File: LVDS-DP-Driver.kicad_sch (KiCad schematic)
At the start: 122 parts, among them J1 47272-0001, J2 Conn_02x15_Odd_Even, J3 Conn_01x06_Male, J4 Conn_01x03_Male, J5 Conn_01x04_Male, J6 Conn_01x03_Male, Q1 Si4816BDY, Q10 2N7002, Q2 Si4816BDY, Q3 Si4816BDY, Q4 MMBT3904, Q5 MMBT3904, Q6 2N7002, Q7 AO3401A, Q8 2N7002, Q9 2N7002, SW1 SW_DIP_x04, U1 CS5211, U2 LTC3853, U3 AT24C64

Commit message: created subschem and C project
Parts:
- J1: footprint Footprints:MOLEX_47272-0001 -> MOLEX_47272-0001
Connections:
- net +3V3 is gone; now on net +3.3V: C10.2, C11.1, C12.1, C37.1, C38.1, C39.1, L1.2, R8.2, R9.1, U1.18 (LVDD), U1.32 (LVDD), U1.52 (LVDD), U2.6 (SENSE2-)
- net GND: no longer SW1.5, SW1.6, SW1.7, U1.63 (GND)
- net GPIO1: no longer SW1.2
- net GPIO2: no longer SW1.3
- net GPIO3: no longer SW1.4
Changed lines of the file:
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@@
   (junction (at 93.345 85.09) (diameter 0) (color 0 0 0 0)
   )
-  (junction (at 212.09 143.51) (diameter 0) (color 0 0 0 0)
-  )
   (junction (at 264.16 105.41) (diameter 0) (color 0 0 0 0)
   )
@@
   (junction (at 33.02 66.04) (diameter 0) (color 0 0 0 0)
   )
-  (junction (at 212.09 139.7) (diameter 0) (color 0 0 0 0)
-  )
-  (junction (at 212.09 141.605) (diameter 0) (color 0 0 0 0)
-  )
   (junction (at 269.24 108.585) (diameter 0) (color 0 0 0 0)
   )
@@
     (stroke (width 0) (type default))
   )
-  (wire (pts (xy 212.09 137.795) (xy 212.09 139.7))
-    (stroke (width 0) (type default))
-  )
   (wire (pts (xy 212.09 78.105) (xy 212.09 84.455))
     (stroke (width 0) (type default))
@@
     (stroke (width 0) (type default))
   )
-  (wire (pts (xy 212.09 141.605) (xy 212.09 143.51))
-    (stroke (width 0) (type default))
-  )
-  (wire (pts (xy 212.09 139.7) (xy 212.09 141.605))
+  (wire (pts (xy 212.09 137.795) (xy 212.09 143.51))
     (stroke (width 0) (type default))
   )
@@
     )
   )
-  (symbol (lib_name "+3.3V_6") (lib_id "power:+3.3V") (at 93.345 85.09 90) (unit 1)
+  (symbol (lib_id "power:+3.3V") (at 93.345 85.09 90) (unit 1)
     (in_bom yes) (on_board yes) (dnp no)
     (property "Reference" "#PWR031" (at 97.155 85.09 0)
@@
     )
   )
-  (symbol (lib_name "+3.3V_7") (lib_id "power:+3.3V") (at 108.585 77.47 0) (unit 1)
+  (symbol (lib_id "power:+3.3V") (at 108.585 77.47 0) (unit 1)
     (in_bom yes) (on_board yes) (dnp no)
     (property "Reference" "#PWR032" (at 108.585 81.28 0)
@@
     (pin "46")
     (pin "47")
-    (pin "47")
     (pin "48")
     (pin "49")
@@
     (pin "52")
     (pin "60")
-    (pin "63")
     (pin "66")
     (pin "67")
@@
     )
   )
-  (symbol (lib_name "+3.3V_4") (lib_id "power:+3.3V") (at 31.115 179.07 0) (unit 1)
+  (symbol (lib_id "power:+3.3V") (at 31.115 179.07 0) (unit 1)
     (in_bom yes) (on_board yes) (dnp no) (fields_autoplaced)
     (property "Reference" "#PWR028" (at 31.115 182.88 0)
@@
     )
   )
-  (symbol (lib_name "+3.3V_3") (lib_id "power:+3.3V") (at 23.495 97.155 270) (unit 1)
+  (symbol (lib_id "power:+3.3V") (at 23.495 97.155 270) (unit 1)
     (in_bom yes) (on_board yes) (dnp no)
     (property "Reference" "#PWR022" (at 19.685 97.155 0)
@@
     )
   )
-  (symbol (lib_name "+3.3V_1") (lib_id "power:+3.3V") (at 160.02 120.65 0) (unit 1)
+  (symbol (lib_id "power:+3.3V") (at 160.02 120.65 0) (unit 1)
     (in_bom yes) (on_board yes) (dnp no)
     (property "Reference" "#PWR0127" (at 160.02 124.46 0)
@@
     )
   )
-  (symbol (lib_name "+3.3V_1") (lib_id "power:+3.3V") (at 133.985 120.65 0) (unit 1)
+  (symbol (lib_id "power:+3.3V") (at 133.985 120.65 0) (unit 1)
     (in_bom yes) (on_board yes) (dnp no)
     (property "Reference" "#PWR0129" (at 133.985 124.46 0)
@@
     )
   )
-  (symbol (lib_name "+3.3V_2") (lib_id "power:+3.3V") (at 31.75 158.115 0) (unit 1)
+  (symbol (lib_id "power:+3.3V") (at 31.75 158.115 0) (unit 1)
     (in_bom yes) (on_board yes) (dnp no) (fields_autoplaced)
     (property "Reference" "#PWR021" (at 31.75 161.925 0)
@@
     )
   )
-  (symbol (lib_name "+3.3V_5") (lib_id "power:+3.3V") (at 81.28 170.815 0) (unit 1)
+  (symbol (lib_id "power:+3.3V") (at 81.28 170.815 0) (unit 1)
     (in_bom yes) (on_board yes) (dnp no) (fields_autoplaced)
     (property "Reference" "#PWR029" (at 81.28 174.625 0)
@@
       (effects (font (size 1.27 1.27)))
     )
-    (property "Footprint" "Footprints:MOLEX_47272-0001" (at 19.05 45.72 0)
+    (property "Footprint" "MOLEX_47272-0001" (at 19.05 45.72 0)
       (effects (font (size 1.27 1.27)) (justify right bottom) hide)
     )
@@
       (project "LVDS-DP-Driver"
         (path "/46838880-46e6-40b4-8167-4d1ff56fb624"
-          (reference "J1") (unit 1) (value "47272-0001") (footprint "Footprints:MOLEX_47272-0001")
+          (reference "J1") (unit 1) (value "47272-0001") (footprint "MOLEX_47272-0001")
         )
       )
@@
     )
   )
-  (symbol (lib_id "power:+3.3V") (at 249.555 82.55 270) (unit 1)
+  (symbol (lib_name "+3.3V_8") (lib_id "power:+3.3V") (at 249.555 82.55 270) (unit 1)
     (in_bom yes) (on_board yes) (dnp no)
     (property "Reference" "#PWR09" (at 245.745 82.55 0)
@@
     )
   )
-  (symbol (lib_name "+3.3V_5") (lib_id "power:+3.3V") (at 110.49 170.815 0) (unit 1)
+  (symbol (lib_id "power:+3.3V") (at 110.49 170.815 0) (unit 1)
     (in_bom yes) (on_board yes) (dnp no) (fields_autoplaced)
     (property "Reference" "#PWR0139" (at 110.49 174.625 0)
@@
     )
   )
-  (symbol (lib_name "+3.3V_1") (lib_id "power:+3.3V") (at 179.705 130.81 0) (unit 1)
+  (symbol (lib_id "power:+3.3V") (at 179.705 130.81 0) (unit 1)
     (in_bom yes) (on_board yes) (dnp no)
     (property "Reference" "#PWR018" (at 179.705 134.62 0)
@@
     )
   )
-  (symbol (lib_name "+3.3V_7") (lib_id "power:+3.3V") (at 118.745 75.565 0) (unit 1)
+  (symbol (lib_id "power:+3.3V") (at 118.745 75.565 0) (unit 1)
     (in_bom yes) (on_board yes) (dnp no)
     (property "Reference" "#PWR0108" (at 118.745 79.375 0)
@@
     )
   )
-  (symbol (lib_name "+3.3V_5") (lib_id "power:+3.3V") (at 139.065 170.815 0) (unit 1)
+  (symbol (lib_id "power:+3.3V") (at 139.065 170.815 0) (unit 1)
     (in_bom yes) (on_board yes) (dnp no) (fields_autoplaced)
     (property "Reference" "#PWR0137" (at 139.065 174.625 0)
@@
     (pin "46")
     (pin "47")
-    (pin "47")
     (pin "48")

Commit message: cleanup and reconstruct
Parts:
- removed C12, C14, C26: 330uF, Capacitor_Tantalum_SMD:CP_EIA-7343-31_Kemet-D, symbol Device:C_Polarized_Small
- removed C20: 330pF, Capacitor_SMD:C_0603_1608Metric, symbol Device:C_Small
- removed C21: 1.5nF, Capacitor_SMD:C_0603_1608Metric, symbol Device:C_Small
- removed C8: 4.7uF, Capacitor_Tantalum_SMD:CP_EIA-3528-21_Kemet-B, symbol Device:C_Polarized_Small
- removed D1, D2, D3: D_Schottky, Diode_SMD:D_SOD-523, symbol Device:D_Schottky
- removed Q1, Q2, Q3: Si4816BDY, Package_SO:SO-8_3.9x4.9mm_P1.27mm, symbol Symbols:Si4816BDY
- removed SW1: SW_DIP_x04, Button_Switch_THT:SW_DIP_SPSTx04_Slide_6.7x11.72mm_W7.62mm_P2.54mm_LowProfile, symbol Switch:SW_DIP_x04
- removed U2: LTC3853, Package_DFN_QFN:QFN-40-1EP_6x6mm_P0.5mm_EP4.6x4.6mm, symbol Symbols:LTC3853
- added C12: 6.8nF, Capacitor_SMD:C_0603_1608Metric, symbol Device:C_Small
- added C14, C56, C61, C64: 100nF, Capacitor_SMD:C_0603_1608Metric, symbol Device:C_Small
- added C20, C21: 47uF, Capacitor_SMD:C_1210_3225Metric, symbol Device:C_Polarized_Small
- added C26, C58: 2.2uF, Capacitor_SMD:C_0603_1608Metric, symbol Device:C_Small
- added C52: 4.7nF, Capacitor_SMD:C_0603_1608Metric, symbol Device:C_Small
- added C53, C54, C63: 10uF, Capacitor_SMD:C_0603_1608Metric, symbol Device:C_Small
- added C55: 3.3nF, Capacitor_SMD:C_0603_1608Metric, symbol Device:C_Small
- added C57: 33pF, Capacitor_SMD:C_0603_1608Metric, symbol Device:C_Small
- added C59: 39nF, Capacitor_SMD:C_0603_1608Metric, symbol Device:C_Small
- added C60: 220nF, Capacitor_SMD:C_0603_1608Metric, symbol Device:C_Small
- added C62: 220pF, Capacitor_SMD:C_0603_1608Metric, symbol Device:C_Small
- added C65: 22uF, Capacitor_SMD:C_0603_1608Metric, symbol Device:C_Small
- added C8: 10uF * 3, Capacitor_SMD:C_2220_5650Metric, symbol Device:C_Small
- added D1: MBR180S1-7, symbol Device:D_Small
- added D2, D6, D7: DSK12, Diode_SMD:D_SOD-123F, symbol Device:D_Schottky_Small
- added D3: RB160MM-90TR, Diode_SMD:D_SOD-123F, symbol Device:D_Schottky_Small
- added L4: CKST353220-2.2uH/M, symbol Device:L_Small
- added Q1, Q11, Q2, Q3: AGM612AP, symbol Device:Q_NMOS_GSD
- added Q12, Q13, Q14, Q15: AGM308AP, symbol Device:Q_NMOS_GSD
- added R54: 10R, symbol Device:R_Small
- added R55: 2K32, symbol Device:R_Small
- added R56: 10K, symbol Device:R_Small
- added R57: 187K, symbol Device:R_Small
- added R58: 150K, symbol Device:R_Small
- added RN1: R_Pack04, symbol Device:R_Pack04
- added U2: LM5176, symbol Symbols:LM5176
- added U5, U8: LM25141, symbol Symbols:LM25141
- added U9: TLV62130, symbol Symbols:TLV62130
- C10: value 100nF -> 15nF
- C11: value 10pF -> 100pF
- C13: value 100nF -> 82pF
- C15: value 10pF -> 47pF
- C16: value 220pF -> 100nF
- C17: value 1.5nF -> 100nF
- C18: value 220pF -> 1uF
- C19: value 1.5nF -> 22uF * 3; footprint Capacitor_SMD:C_0603_1608Metric -> Capacitor_SMD:C_0805_2012Metric
- C22: value 100nF -> 10uF
- C24: value 100nF -> 39nF
- C25: value 68nF -> 220nF
- C28: value 100nF -> 4.7uF
- C29: value 100nF -> 56pF
- C7: value 22uF -> 68uF; footprint Capacitor_Tantalum_SMD:CP_EIA-3528-21_Kemet-B -> Capacitor_THT:CP_Radial_D6.3mm_P2.50mm
- C9: value 1nF -> 100nF
- J1: footprint MOLEX_47272-0001 -> Footprints:MOLEX_47272-0001
- L1: value 3.3uH -> CYA0650-3.3UH; footprint Inductor_SMD:L_7.3x7.3_H4.5 -> (none)
- L2: value 3.3uH -> CKST353220-2.2uH/M; footprint Inductor_SMD:L_7.3x7.3_H4.5 -> (none)
- L3: value 1.5uH -> CKST322512-1uH/M; footprint Inductor_SMD:L_1210_3225Metric -> (none)
- R10: value 20K -> 93K1; footprint Resistor_SMD:R_0603_1608Metric -> (none)
- R11: value 4.75K -> 13K; footprint Resistor_SMD:R_0603_1608Metric -> (none)
- R12: value 1430 -> 15m; footprint Resistor_SMD:R_1206_3216Metric -> (none)
- R13: value 105K -> 100R; footprint Resistor_SMD:R_0603_1608Metric -> (none)
- R14: value 20K -> 100R; footprint Resistor_SMD:R_0603_1608Metric -> (none)
- R15: value 15K -> 10K; footprint Resistor_SMD:R_0603_1608Metric -> (none)
- R16: value 18K -> 280K; footprint Resistor_SMD:R_0603_1608Metric -> (none)
- R17: value 10K -> 280K; footprint Resistor_SMD:R_0603_1608Metric -> (none)
- R18: value 2.43K -> 10R; footprint Resistor_SMD:R_0603_1608Metric -> (none)
- R19: value 1.82K -> 12m; footprint Resistor_SMD:R_0603_1608Metric -> (none)
- R20: value 25K -> 1K62; footprint Resistor_SMD:R_0603_1608Metric -> (none)
- R21: value 20K -> 10m; footprint Resistor_SMD:R_0603_1608Metric -> (none)
- R5: value 10K -> 249K; footprint Resistor_SMD:R_0603_1608Metric -> (none)
- R6: value 3.16K -> 42K2; footprint Resistor_SMD:R_0603_1608Metric -> (none)
- R7: value 4.75K -> 2K; footprint Resistor_SMD:R_0603_1608Metric -> (none)
- R8: value 1430 -> 10R; footprint Resistor_SMD:R_1206_3216Metric -> (none)
- R9: value 63.4K -> 6K19; footprint Resistor_SMD:R_0603_1608Metric -> (none)
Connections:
- net +12V: now also C19.1, C22.1, R16.1, C20.1, C21.1, C53.1, C63.1, C64.1, Q12.3 (D), Q14.3 (D), Q3.3 (D), U2.12 (VOSNS), U5.15 (VIN), U5.23 (EN), U8.15 (VIN), U8.23 (EN), U9.10 (AVIN), U9.11 (PVIN), U9.12 (PVIN), U9.13 (EN); no longer C7.1
- net +1V8: now also C65.1, L4.2, R56.1, R57.1, U9.14 (VOS); no longer C25.2, L3.2, R19.2, R20.1
- net +3.3V: no longer C10.2, C11.1, L1.2, R8.2, R9.1
- net +5V: now also C28.1, R19.2, U5.17 (VOUT), U8.17 (VOUT); no longer C13.2, C15.1, L2.2, R12.2, R13.1
- net GND: now also C10.1, C11.1, C13.2, C23.2, C24.2, C25.2, C28.2, C29.2, R10.1, R11.1, R12.1, R13.1, R17.2, R20.2, R9.1, C14.2, C20.2, C21.2, C26.2, C53.2, C54.2, C57.2, C58.2, C59.2, C60.2, C61.2, C62.1, C63.2, C64.2, C65.2, C8.2, Q13.2 (S), Q15.2 (S), R55.2, R58.2, RN1.1 (R1.1), RN1.2 (R2.1), RN1.3 (R3.1), RN1.4 (R4.1), U2.10 (AGND), U2.13 (ISNS-), U2.14 (ISNS+), U2.22 (PGND), U2.5 (DITH), U5.16 (VCCX), U5.19 (FB), U5.3 (AGND), U5.9 (PGND), U8.16 (VCCX), U8.3 (AGND), U8.9 (PGND), U9.15 (PGND), U9.16 (PGND), U9.17 (PGND), U9.6 (AGND), U9.7 (FSW); no longer C16.2, C17.2, C23.1, C24.1, R10.2, R14.2, R21.2
- net GPIO0: now also RN1.5 (R4.2)
- net GPIO1: now also RN1.6 (R3.2)
- net GPIO2: now also RN1.7 (R2.2)
- net GPIO3: now also RN1.8 (R1.2)
- net ENABLE: now reaches R5.2, R6.1
- net ENABLE: now also U2.1 (EN); no longer C9.1
- net MAINPWR_FB: now reaches R17.1
- net MAINPWR_FB: now also R16.2, U2.11 (FB)
- net BUCK5_SW: now reaches C27.1
- net BUCK5_SW: now also L2.1, Q12.2 (S), Q13.3 (D), U5.12 (SW)
- net VDC: now reaches R5.1
- net VDC: now also C7.1, R7.1, C8.1, D1.2 (A), Q1.3 (D)
- net VCC: now reaches C18.1
- net VCC: now also R15.1, D2.2 (A), D3.2 (A), U2.23 (VCC); no longer R16.1
- net at C29.1: now also C52.1, U5.20 (COMP)
- net at C17.1: now also D3.1 (K), U2.26 (BOOT1); no longer R15.2
- net SW2: now reaches C16.1
- net SW2: now also L1.2, Q11.3 (D), Q3.2 (S), U2.18 (SW2); no longer R15.1
- removed net FB1: C15.2, R13.2, R14.1
- removed net FB2: C11.2, R10.1, R9.2
- net FB3 renamed CS_3
- net CS_3: now also L3.2, U8.18 (CS); no longer R20.2
- removed net SEN1+: C13.1, R11.2, R12.1
- removed net SEN2+: C10.1, R7.2, R8.1
- removed net SEN3+: C25.1, R18.2, R19.1
- removed net SW3: C29.2, L3.1, R18.1
- new net: C13.1, U2.7 (SLOPE)
- new net: C12.1, R9.2
- new net: C10.2, U2.8 (SS)
- new net: R54.1, U8.13 (HO)
- new net: C25.1, U5.24 (RES)
- new net: C56.2, D7.1 (K), U8.11 (HB)
- new net: R56.2, U9.4 (PG)
- new net: C62.2, U9.9 (SS)
- new net: C27.2, D6.1 (K), U5.11 (HB)
- new net: C52.2, R20.1
- new net: C11.2, C12.2, U2.9 (COMP)
- new net: R11.2, U2.6 (SYNC)
- new net: C59.1, U8.22 (SS)
- new net: C15.2, R14.2, U2.16 (CS)
- new net: R57.2, R58.1, U9.5 (FB)
- new net: R18.1, U5.13 (HO)
- new net: C60.1, U8.24 (RES)
- new net: C9.1, R8.2, U2.2 (VIN)
- new net: C23.1, U5.1 (DEMB), U5.2 (VDDA), U5.5 (DITH), U5.6 (OSC)
- new net: C24.1, U5.22 (SS)
- new net: L4.1, U9.1 (SW), U9.2 (SW), U9.3 (SW)
- new net: R10.2, U2.4 (MODE)
- new net: C55.1, C57.1, U8.20 (COMP)
- new net: C16.2, D2.1 (K), U2.20 (BOOT2)
- new net: D1.1 (K), R8.1
- new net: C55.2, R55.1
- new net: C15.1, R13.2, U2.15 (CSG)
- new net: C14.1, U2.24 (BIAS)
- new net +3V3: C54.1, R21.2
- new net BUCK3_BIASVCC: C58.1, D7.2 (A), U8.10 (VCC)
- new net BUCK3_SW: C56.1, L3.1, Q14.2 (S), Q15.3 (D), U8.12 (SW)
- new net BUCK5_BIASVCC: C26.1, D6.2 (A), U5.10 (VCC)
- new net CS_5: L2.2, R19.1, U5.18 (CS)
- new net FB_3: C61.1, U8.1 (DEMB), U8.19 (FB), U8.2 (VDDA), U8.5 (DITH), U8.6 (OSC)
- new net HDRV1: Q1.1 (G), U2.27 (HDRV1)
- new net HDRV2: Q3.1 (G), U2.19 (HDRV2)
- new net HDRV_3: Q14.1 (G), R54.2, U8.14 (HOL)
- new net HDRV_5: Q12.1 (G), R18.2, U5.14 (HOL)
- new net LDRV1: Q2.1 (G), U2.25 (LDRV1)
- new net LDRV2: Q11.1 (G), U2.21 (LDRV2)
- new net LDRV_3: Q15.1 (G), U8.7 (LOL), U8.8 (LO)
- new net LDRV_5: Q13.1 (G), U5.7 (LOL), U5.8 (LO)
- new net MAIN_PG: R15.2, U2.17 (PG)
- new net RCS: Q11.2 (S), Q2.2 (S), R12.2, R14.1
- new net SW1: C17.2, L1.1, Q1.2 (S), Q2.3 (D), U2.28 (SW1)
- new net VINSNS: R7.2, U2.3 (VISNS)
- no-connect marks 14 -> 17
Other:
- note added: "FS55X106K101EGG"
- note added: "SPT1HM680E09ORVZC"
- note added: "同焊盘堆叠焊接"
- moved on the sheet: C1, C2, C3, C30, C31, C32, C33, C34, C35, C36, C37, C38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

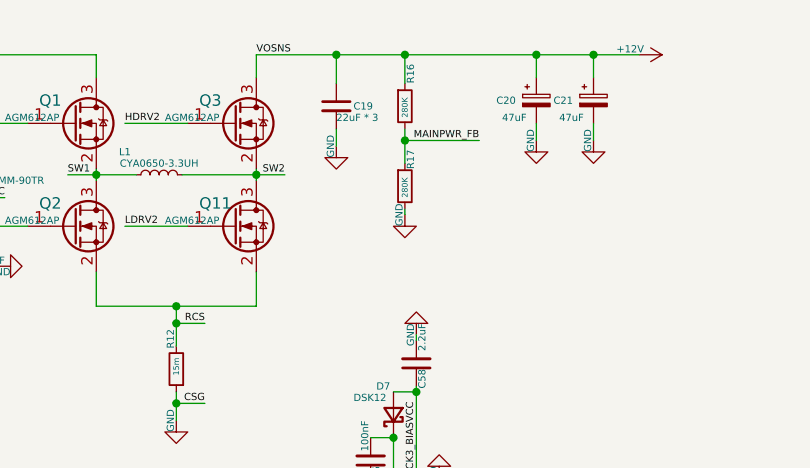
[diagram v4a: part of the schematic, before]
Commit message: assigned footprints
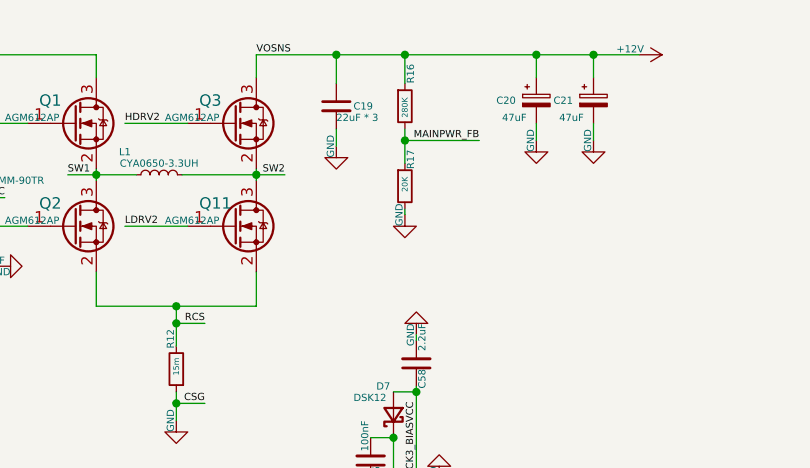
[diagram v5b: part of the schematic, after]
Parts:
- D1: footprint (none) -> Diode_SMD:D_SMA
- L1: footprint (none) -> Footprints:L_0530
- L2, L4: footprint (none) -> Footprints:CKST353220
- L3: footprint (none) -> Footprints:CKST322512
- Q1, Q11, Q12, Q13, Q14, Q15, Q2, Q3: footprint (none) -> Footprints:PDFN8_3x3
- R10, R11, R13, R14, R15, R5, R6, R7, R8, R9: footprint (none) -> Resistor_SMD:R_0603_1608Metric
- R12: footprint (none) -> Resistor_SMD:R_0805_2012Metric
- R17: value 280K -> 20K
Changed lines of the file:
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@@
       (effects (font (size 0.64 0.64)) (justify left))
     )
-    (property "Footprint" "" (at 224.155 51.435 0)
+    (property "Footprint" "Resistor_SMD:R_0805_2012Metric" (at 224.155 51.435 0)
       (effects (font (size 1.27 1.27)) hide)
     )
@@
       (effects (font (size 0.64 0.64)) (justify left))
     )
-    (property "Footprint" "" (at 153.035 40.005 0)
+    (property "Footprint" "Resistor_SMD:R_0603_1608Metric" (at 153.035 40.005 0)
       (effects (font (size 1.27 1.27)) hide)
     )
@@
       (effects (font (size 0.8 0.8)) (justify left))
     )
-    (property "Value" "280K" (at 249.555 32.385 90)
+    (property "Value" "20K" (at 249.555 31.75 90)
       (effects (font (size 0.64 0.64)) (justify left))
     )
@@
       (effects (font (size 0.64 0.64)) (justify left))
     )
-    (property "Footprint" "" (at 198.755 55.245 0)
+    (property "Footprint" "Resistor_SMD:R_0603_1608Metric" (at 198.755 55.245 0)
       (effects (font (size 1.27 1.27)) hide)
     )
@@
       (effects (font (size 0.64 0.64)) (justify left))
     )
-    (property "Footprint" "" (at 169.545 40.005 0)
+    (property "Footprint" "Resistor_SMD:R_0603_1608Metric" (at 169.545 40.005 0)
       (effects (font (size 1.27 1.27)) hide)
     )
@@
       (effects (font (size 0.8 0.8)))
     )
-    (property "Footprint" "" (at 134.62 86.36 0)
+    (property "Footprint" "Footprints:CKST353220" (at 134.62 86.36 0)
       (effects (font (size 1.27 1.27)) hide)
     )
@@
       (effects (font (size 0.64 0.64)) (justify left))
     )
-    (property "Footprint" "" (at 200.66 64.77 0)
+    (property "Footprint" "Resistor_SMD:R_0603_1608Metric" (at 200.66 64.77 0)
       (effects (font (size 1.27 1.27)) hide)
     )
@@
       (effects (font (size 0.8 0.8)) (justify left))
     )
-    (property "Footprint" "" (at 217.805 21.59 0)
+    (property "Footprint" "Footprints:PDFN8_3x3" (at 217.805 21.59 0)
       (effects (font (size 1.27 1.27)) hide)
     )
@@
       (effects (font (size 0.8 0.8)) (justify left))
     )
-    (property "Footprint" "" (at 235.585 21.59 0)
+    (property "Footprint" "Footprints:PDFN8_3x3" (at 235.585 21.59 0)
       (effects (font (size 1.27 1.27)) hide)
     )
@@
       (effects (font (size 0.8 0.8)) (justify left))
     )
-    (property "Footprint" "" (at 235.585 33.02 0)
+    (property "Footprint" "Footprints:PDFN8_3x3" (at 235.585 33.02 0)
       (effects (font (size 1.27 1.27)) hide)
     )
@@
       (effects (font (size 0.64 0.64)) (justify left))
     )
-    (property "Footprint" "" (at 151.13 20.32 0)
+    (property "Footprint" "Resistor_SMD:R_0603_1608Metric" (at 151.13 20.32 0)
       (effects (font (size 1.27 1.27)) hide)
     )
@@
       (effects (font (size 0.8 0.8)))
     )
-    (property "Footprint" "" (at 227.965 90.17 0)
+    (property "Footprint" "Footprints:CKST353220" (at 227.965 90.17 0)
       (effects (font (size 1.27 1.27)) hide)
     )
@@
       (effects (font (size 0.8 0.8)) (justify left))
     )
-    (property "Footprint" "" (at 217.805 33.02 0)
+    (property "Footprint" "Footprints:PDFN8_3x3" (at 217.805 33.02 0)
       (effects (font (size 1.27 1.27)) hide)
     )
@@
       (effects (font (size 0.64 0.64)) (justify left))
     )
-    (property "Footprint" "" (at 169.545 34.925 0)
+    (property "Footprint" "Resistor_SMD:R_0603_1608Metric" (at 169.545 34.925 0)
       (effects (font (size 1.27 1.27)) hide)
     )
@@
       (effects (font (size 0.64 0.64)) (justify left))
     )
-    (property "Footprint" "" (at 146.05 25.4 0)
+    (property "Footprint" "Resistor_SMD:R_0603_1608Metric" (at 146.05 25.4 0)
       (effects (font (size 1.27 1.27)) hide)
     )
@@
       (effects (font (size 0.8 0.8)))
     )
-    (property "Footprint" "" (at 221.615 127 0)
+    (property "Footprint" "Footprints:CKST322512" (at 221.615 127 0)
       (effects (font (size 1.27 1.27)) hide)
     )
@@
       (effects (font (size 0.64 0.64)) (justify left))
     )
-    (property "Footprint" "" (at 155.575 26.035 0)
+    (property "Footprint" "Resistor_SMD:R_0603_1608Metric" (at 155.575 26.035 0)
       (effects (font (size 1.27 1.27)) hide)
     )
@@
       (effects (font (size 0.8 0.8)) (justify left))
     )
-    (property "Footprint" "" (at 130.175 89.535 0)
+    (property "Footprint" "Footprints:PDFN8_3x3" (at 130.175 89.535 0)
       (effects (font (size 1.27 1.27)) hide)
     )
@@
       (effects (font (size 0.64 0.64)) (justify left))
     )
-    (property "Footprint" "" (at 192.405 64.77 0)
+    (property "Footprint" "Resistor_SMD:R_0603_1608Metric" (at 192.405 64.77 0)
       (effects (font (size 1.27 1.27)) hide)
     )
@@
       (effects (font (size 0.64 0.64)) (justify left))
     )
-    (property "Footprint" "" (at 146.05 19.05 0)
+    (property "Footprint" "Resistor_SMD:R_0603_1608Metric" (at 146.05 19.05 0)
       (effects (font (size 1.27 1.27)) hide)
     )
@@
       (effects (font (size 0.8 0.8)) (justify left))
     )
-    (property "Footprint" "" (at 130.175 78.105 0)
+    (property "Footprint" "Footprints:PDFN8_3x3" (at 130.175 78.105 0)
       (effects (font (size 1.27 1.27)) hide)
     )
@@
       (effects (font (size 0.8 0.8)))
     )
-    (property "Footprint" "" (at 222.25 29.845 0)
+    (property "Footprint" "Footprints:L_0530" (at 222.25 29.845 0)
       (effects (font (size 1.27 1.27)) hide)
     )
@@
       (effects (font (size 0.64 0.64)) (justify right))
     )
-    (property "Footprint" "" (at 155.575 19.685 90)
+    (property "Footprint" "Diode_SMD:D_SMA" (at 155.575 19.685 90)
       (effects (font (size 1.27 1.27)) hide)
     )
@@
       (effects (font (size 0.8 0.8)) (justify left))
     )
-    (property "Footprint" "" (at 217.17 118.745 0)
+    (property "Footprint" "Footprints:PDFN8_3x3" (at 217.17 118.745 0)
       (effects (font (size 1.27 1.27)) hide)
     )
@@
       (effects (font (size 0.8 0.8)) (justify left))
     )
-    (property "Footprint" "" (at 217.17 130.175 0)
+    (property "Footprint" "Footprints:PDFN8_3x3" (at 217.17 130.175 0)
       (effects (font (size 1.27 1.27)) hide)
     )

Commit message: reconstruct
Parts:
- removed R15: 10K, Resistor_SMD:R_0603_1608Metric, symbol Device:R_Small
- D1: value MBR180S1-7 -> MBR0580S1-7; footprint Diode_SMD:D_SMA -> Diode_SMD:D_SOD-123
- D2: value DSK12 -> B5817WS-MS; footprint Diode_SMD:D_SOD-123F -> Diode_SMD:D_SOD-323
- D3: value RB160MM-90TR -> B110WS; footprint Diode_SMD:D_SOD-123F -> Diode_SMD:D_SOD-323
- R16, R17, R18, R19, R20, R21, R54, R55, R56, R57, R58: footprint (none) -> Resistor_SMD:R_0603_1608Metric
- RN1: footprint (none) -> Resistor_SMD:R_Array_Concave_4x0603
- U2: footprint (none) -> Package_SO:HTSSOP-28-1EP_4.4x9.7mm_P0.65mm_EP2.85x5.4mm
- U5, U8: footprint (none) -> Package_DFN_QFN:VQFN-24-1EP_4x4mm_P0.5mm_EP2.5x2.5mm_ThermalVias
- U9: footprint (none) -> Package_DFN_QFN:VQFN-16-1EP_3x3mm_P0.5mm_EP1.6x1.6mm
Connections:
- net LCD_VCC is gone; now on net HT: J2.1 (Pin_1), J2.2 (Pin_2), J2.3 (Pin_3)
- net +12V: no longer TP3.1
- net +3.3V: no longer J4.3 (Pin_3), Q10.1 (G), Q6.1 (G), R22.1, R27.1, R28.1, R29.1, R30.1, R31.1, R37.1, R39.1, R40.1, R41.1, R42.1, R43.1, R44.1, R45.2, R46.2, U3.8 (VDD)
- net +3V3: now also J4.3 (Pin_3), Q10.1 (G), Q6.1 (G), R22.1, R27.1, R28.1, R29.1, R30.1, R31.1, R37.1, R39.1, R40.1, R41.1, R42.1, R43.1, R44.1, R45.2, R46.2, U3.8 (VDD), U8.17 (VOUT)
- net +5V: no longer U8.17 (VOUT)
- net VDC: now also TP3.1
- net AUXP: now reaches C6.2, U1.44 (AUXP)
- net DP0N: now reaches C1.2, U1.62 (DP0N)
- net DP0P: now reaches C2.2, U1.61 (DP0P)
- net DP1N: now reaches C3.2, U1.65 (DP1N)
- net DP1P: now reaches C4.2, U1.64 (DP1P)
- net AUXN: now reaches C5.2, U1.43 (AUXN)
- net MAIN_PG: no longer names the net of U2.17 (PG)
- no-connect marks 17 -> 18
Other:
- moved on the sheet: C1, C2, C3, C4, C5, C6
